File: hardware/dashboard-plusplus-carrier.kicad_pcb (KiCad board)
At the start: 4 copper layers, 95 x 55 mm, 54 parts, among them J1 XT30U-M, J10a ESP32-DEVKIT-A, J10b ESP32-DEVKIT-B, J13 DEBUG, J14 TRIP + EN, J15 SPARE, J17 IGN + COOLANT, J3 TFT-ILI9488, J6 LDR + FUEL, J8 GPS_PADS, J9 HALL, Q1 IRFR9540N, U4 DPP_DCDC_MODULE

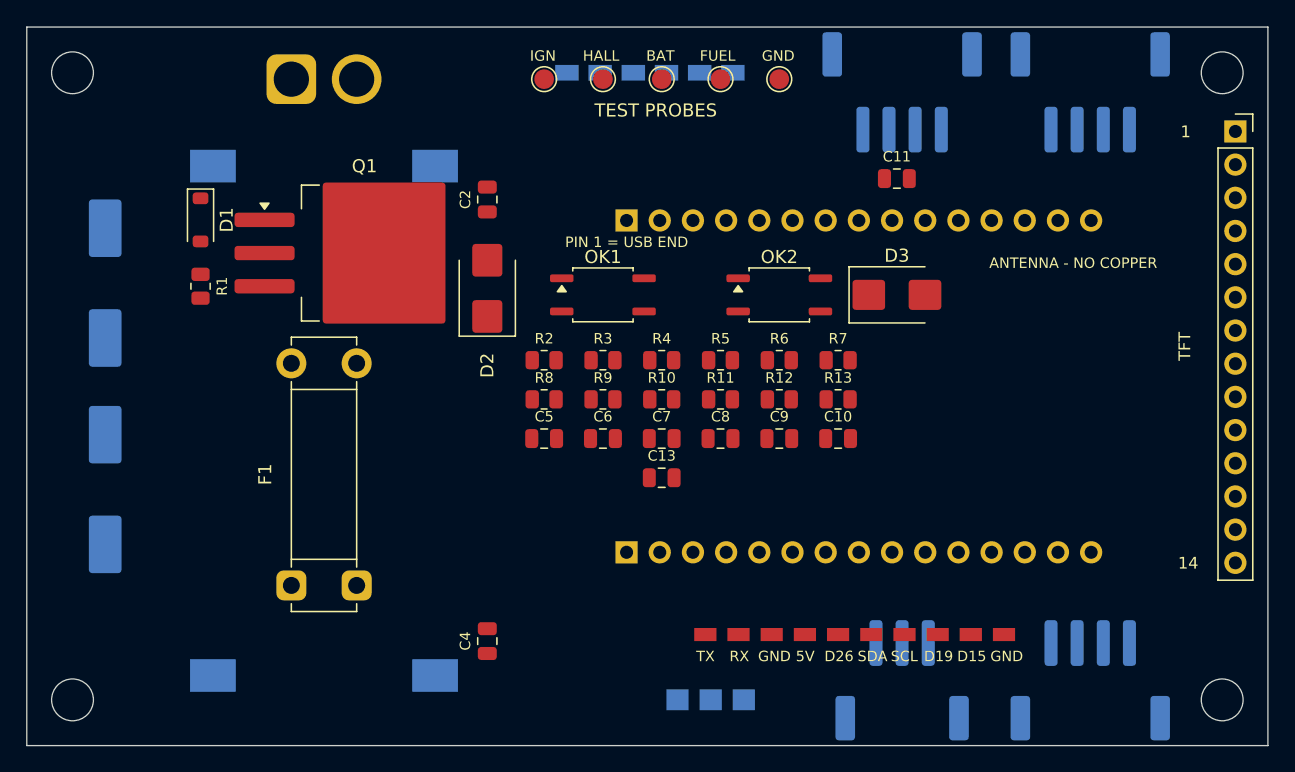
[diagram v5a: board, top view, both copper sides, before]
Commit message: Move F1 4.41 mm south, centre TP row east on x 61.15
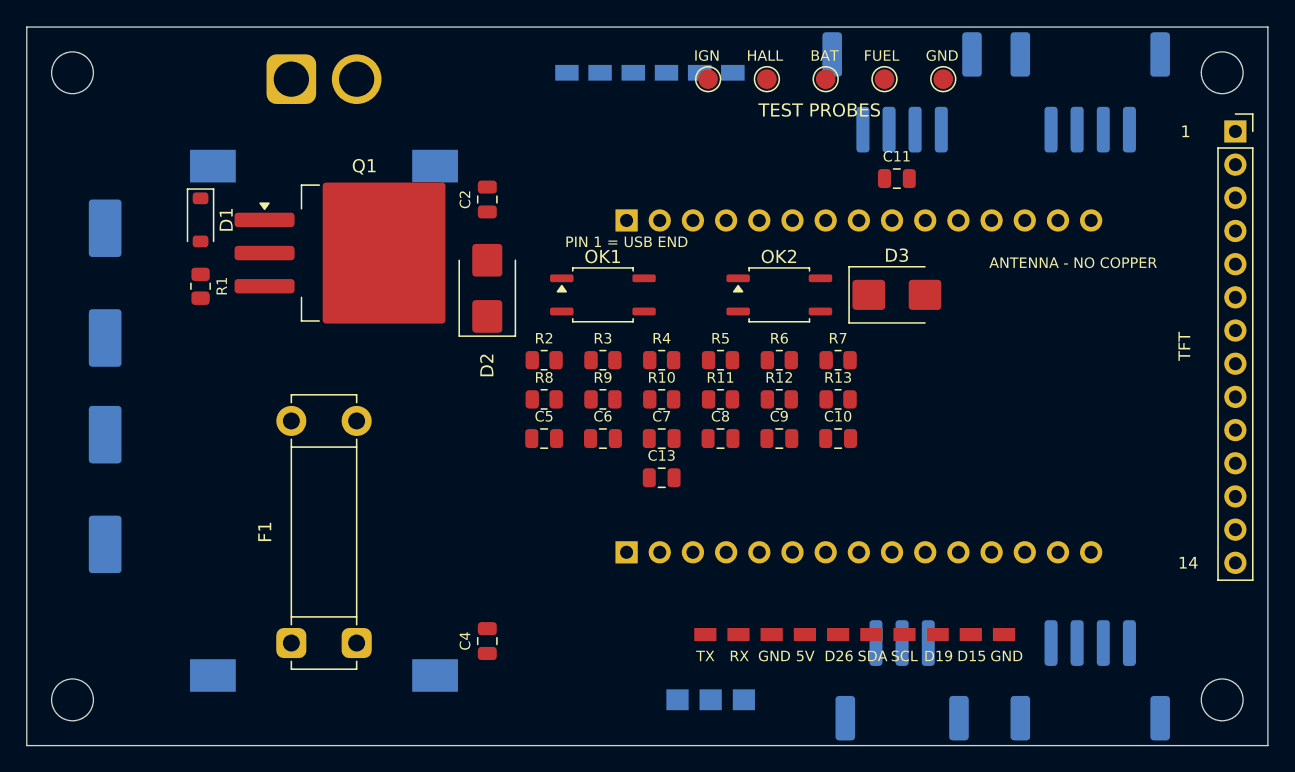
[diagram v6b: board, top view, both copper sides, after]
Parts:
- moved TP1 12.6 mm to (153.2, 81.5)
- moved TP2 12.6 mm to (157.7, 81.5)
- moved TP3 12.6 mm to (162.2, 81.5)
- moved TP4 12.6 mm to (166.7, 81.5)
- moved TP5 12.6 mm to (171.2, 81.5)
- moved F1 4.41 mm to (121.2, 124.7)
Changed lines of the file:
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@@
 (footprint "dpp:Fuseholder_Clip-5x20mm_Littelfuse_521_Lateral_P17.00x5.00mm_D1.30mm_Horizontal"
 	(layer "F.Cu")
-	(at 121.2500 120.2400 90.0)
+	(at 121.2500 124.6500 90.0)
 (descr "Fuseholder Clips, 5x20mm Cylinder Fuse, Pins Inline, Horizontal, Littelfuse 521, https://www.littelfuse.com/~/media/electronics/datasheets/fuse_clips/littelfuse_fuse_clip_520_521_102071_datasheet.pdf.pdf")
 (tags "fuse clip open")
@@
 (footprint "dpp:TestPoint_Pad_D1.5mm"
 	(layer "F.Cu")
-	(at 140.6000 81.4900 0.0)
+	(at 153.1500 81.4900 0.0)
 (descr "SMD pad as test Point, diameter 1.5mm")
 (tags "test point SMD pad")
@@
 (footprint "dpp:TestPoint_Pad_D1.5mm"
 	(layer "F.Cu")
-	(at 145.1000 81.4900 0.0)
+	(at 157.6500 81.4900 0.0)
 (descr "SMD pad as test Point, diameter 1.5mm")
 (tags "test point SMD pad")
@@
 (footprint "dpp:TestPoint_Pad_D1.5mm"
 	(layer "F.Cu")
-	(at 149.6000 81.4900 0.0)
+	(at 162.1500 81.4900 0.0)
 (descr "SMD pad as test Point, diameter 1.5mm")
 (tags "test point SMD pad")
@@
 (footprint "dpp:TestPoint_Pad_D1.5mm"
 	(layer "F.Cu")
-	(at 154.1000 81.4900 0.0)
+	(at 166.6500 81.4900 0.0)
 (descr "SMD pad as test Point, diameter 1.5mm")
 (tags "test point SMD pad")
@@
 (footprint "dpp:TestPoint_Pad_D1.5mm"
 	(layer "F.Cu")
-	(at 158.6000 81.4900 0.0)
+	(at 171.1500 81.4900 0.0)
 (descr "SMD pad as test Point, diameter 1.5mm")
 (tags "test point SMD pad")
@@
 (gr_text "HALL" (at 169.41 120.40 0.0) (layer "B.SilkS") (effects (font (size 0.80 0.80) (thickness 0.12)) (justify left top mirror)))
 (gr_text "GNSS" (at 160.00 80.40 0.0) (layer "B.SilkS") (effects (font (size 0.80 0.80) (thickness 0.12)) (justify left top mirror)))
-(gr_text "IGN" (at 139.51 79.24 0.0) (layer "F.SilkS") (effects (font (size 0.80 0.80) (thickness 0.12)) (justify left top)))
-(gr_text "HALL" (at 143.56 79.24 0.0) (layer "F.SilkS") (effects (font (size 0.80 0.80) (thickness 0.12)) (justify left top)))
-(gr_text "BAT" (at 148.41 79.24 0.0) (layer "F.SilkS") (effects (font (size 0.80 0.80) (thickness 0.12)) (justify left top)))
-(gr_text "FUEL" (at 152.51 79.24 0.0) (layer "F.SilkS") (effects (font (size 0.80 0.80) (thickness 0.12)) (justify left top)))
-(gr_text "GND" (at 157.26 79.24 0.0) (layer "F.SilkS") (effects (font (size 0.80 0.80) (thickness 0.12)) (justify left top)))
-(gr_text "TEST PROBES" (at 144.45 83.30 0.0) (layer "F.SilkS") (effects (font (size 1.00 1.00) (thickness 0.15)) (justify left top)))
+(gr_text "IGN" (at 152.06 79.24 0.0) (layer "F.SilkS") (effects (font (size 0.80 0.80) (thickness 0.12)) (justify left top)))
+(gr_text "HALL" (at 156.10 79.24 0.0) (layer "F.SilkS") (effects (font (size 0.80 0.80) (thickness 0.12)) (justify left top)))
+(gr_text "BAT" (at 160.97 79.24 0.0) (layer "F.SilkS") (effects (font (size 0.80 0.80) (thickness 0.12)) (justify left top)))
+(gr_text "FUEL" (at 165.06 79.24 0.0) (layer "F.SilkS") (effects (font (size 0.80 0.80) (thickness 0.12)) (justify left top)))
+(gr_text "GND" (at 169.81 79.24 0.0) (layer "F.SilkS") (effects (font (size 0.80 0.80) (thickness 0.12)) (justify left top)))
+(gr_text "TEST PROBES" (at 157.00 83.30 0.0) (layer "F.SilkS") (effects (font (size 1.00 1.00) (thickness 0.15)) (justify left top)))
 (gr_text "SDA" (at 143.39 82.90 0.0) (layer "B.SilkS") (effects (font (size 0.80 0.80) (thickness 0.12)) (justify left top mirror)))
 (gr_text "SCL" (at 145.94 82.90 0.0) (layer "B.SilkS") (effects (font (size 0.80 0.80) (thickness 0.12)) (justify left top mirror)))
